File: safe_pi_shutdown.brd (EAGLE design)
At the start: 65 x 56 mm, 33 parts, among them IC1 MCP73831, IC2 LTC2952CF, IC3 MT3608, Q1 IRF7342, Q2 IRF7342, X4 MF-CON-2.54mm-01x02, X5 MF-CON-2.54mm-01x02

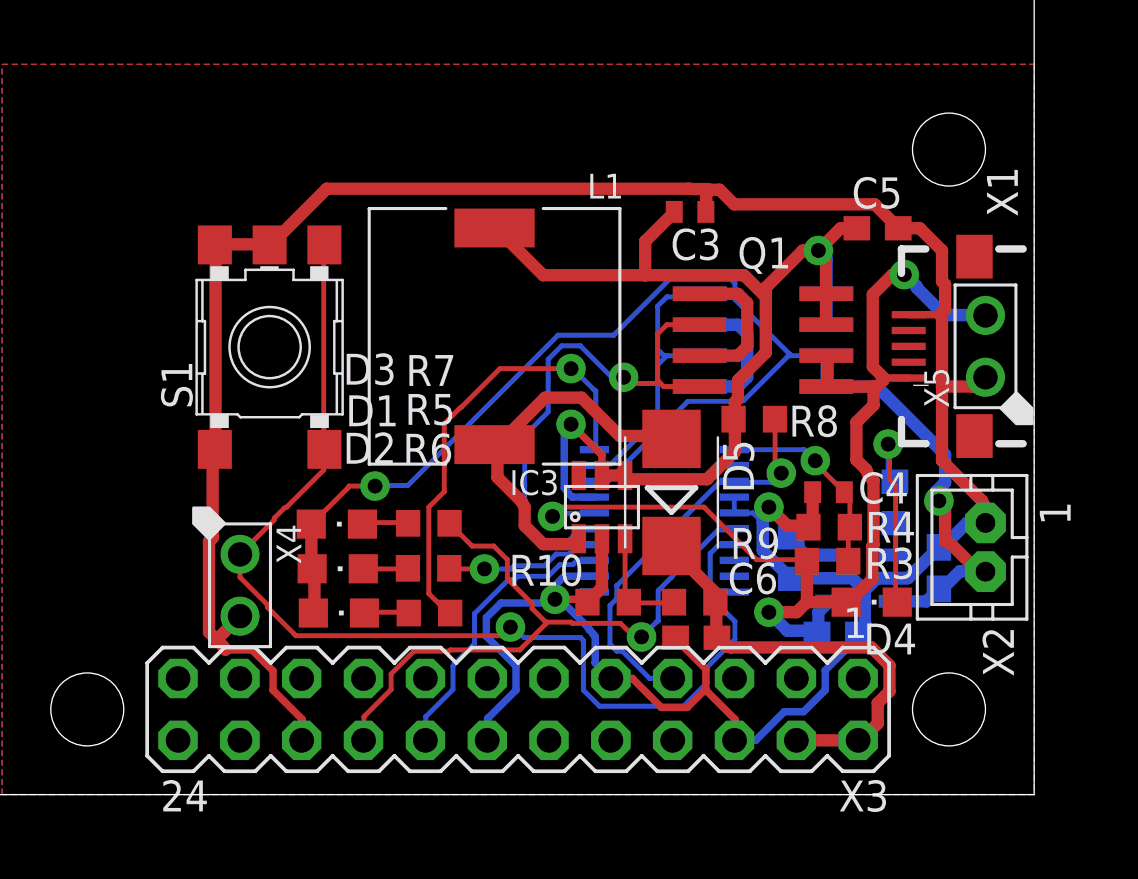
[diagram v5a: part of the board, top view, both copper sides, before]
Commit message: zmiana micro usb, poprawki z kondensatorami i inne
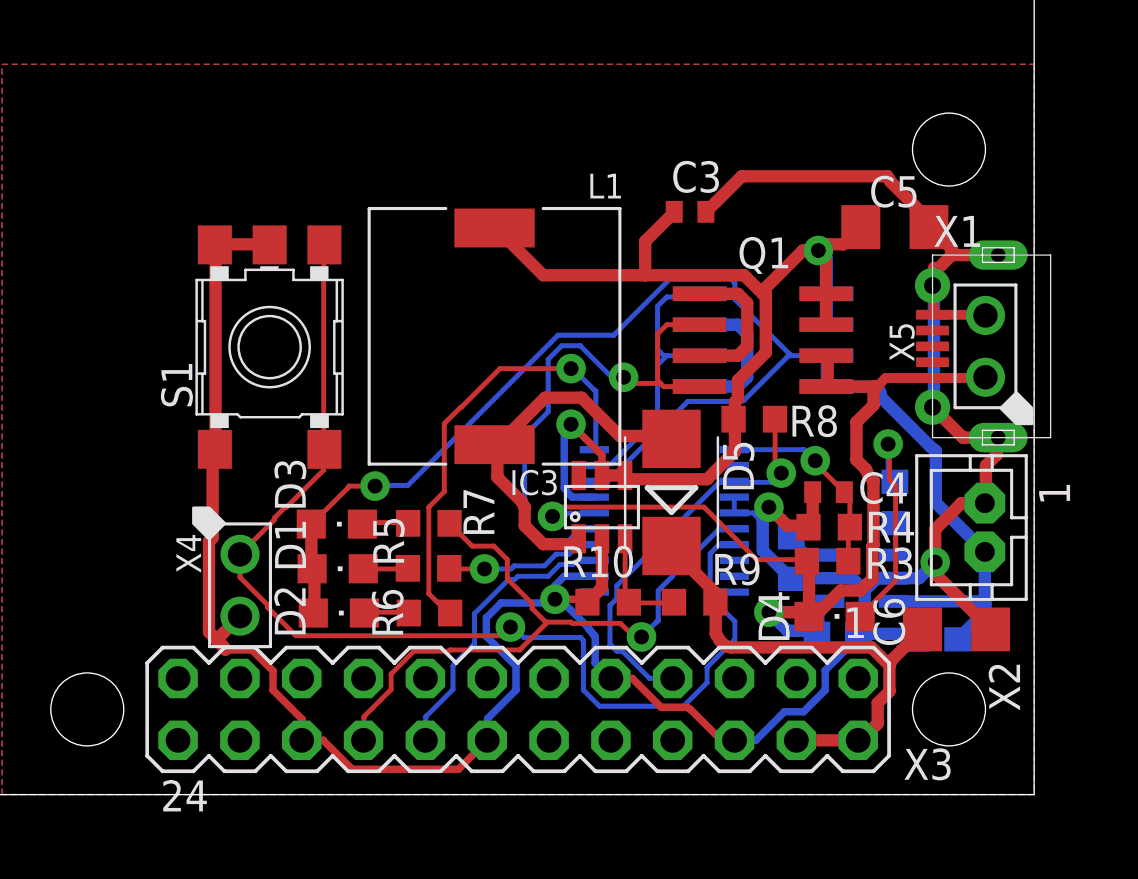
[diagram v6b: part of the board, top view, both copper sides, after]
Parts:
- C5, C6: device rcl:C0603 -> rcl:C1206
- X1: value (none) -> MICRO-USB-RECEPTACLE47589-0001; device MicroUSB:USB-MICRO-SMD -> con-molex-usb:47589-0001
- moved C6 10.7 mm to (61.8, 6.79), turned to 0 degrees
- moved C2 2.93 mm to (61.0, 6.38), turned to 0 degrees
- moved D4 1.63 mm to (56.8, 7.32)
- moved X1 0.98 mm to (63.5, 18.4)
- moved X2 0.81 mm to (63.0, 11.0)
- moved C5 0.71 mm to (59.3, 23.3)
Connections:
- net GND: now also X1.5, X1.CASING1, X1.CASING2, X1.CASING3, X1.CASING4, X5.P$2; no longer X1.GND1, X5.P$1
- net V2: now also X1.1, X5.P$1; no longer X1.VBUS1, X5.P$2
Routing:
- net V2: track 46.5 -> 41.1 mm, vias 3 -> 2
- net GND: track 131.0 -> 128.5 mm, vias 2 -> 3
- net V1: track 58.8 -> 61.0 mm, vias 2 -> 1
- net N$4: track 18.3 -> 20.3 mm
- net N$6: track 8.43 -> 9.59 mm
- net VCC: track 47.3 -> 47.9 mm

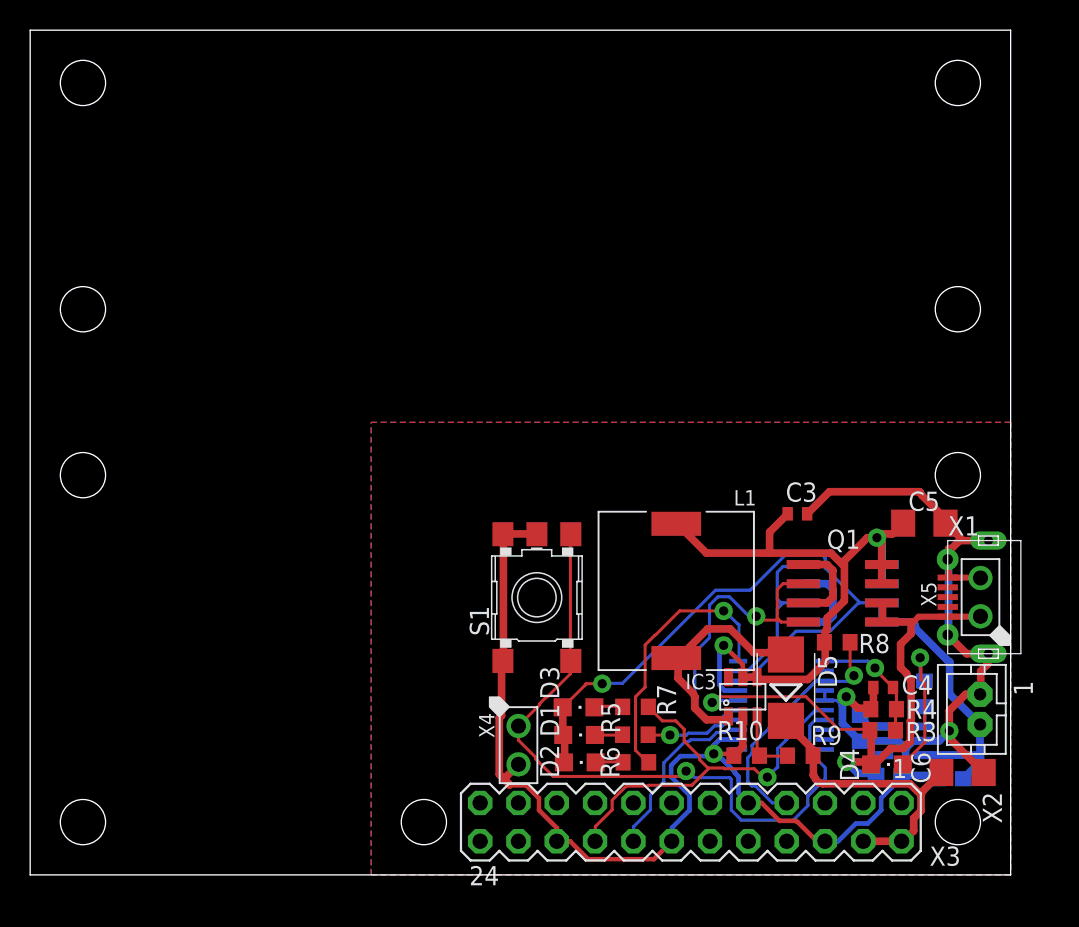
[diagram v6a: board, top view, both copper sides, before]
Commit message: przyciecie plytki do minimum
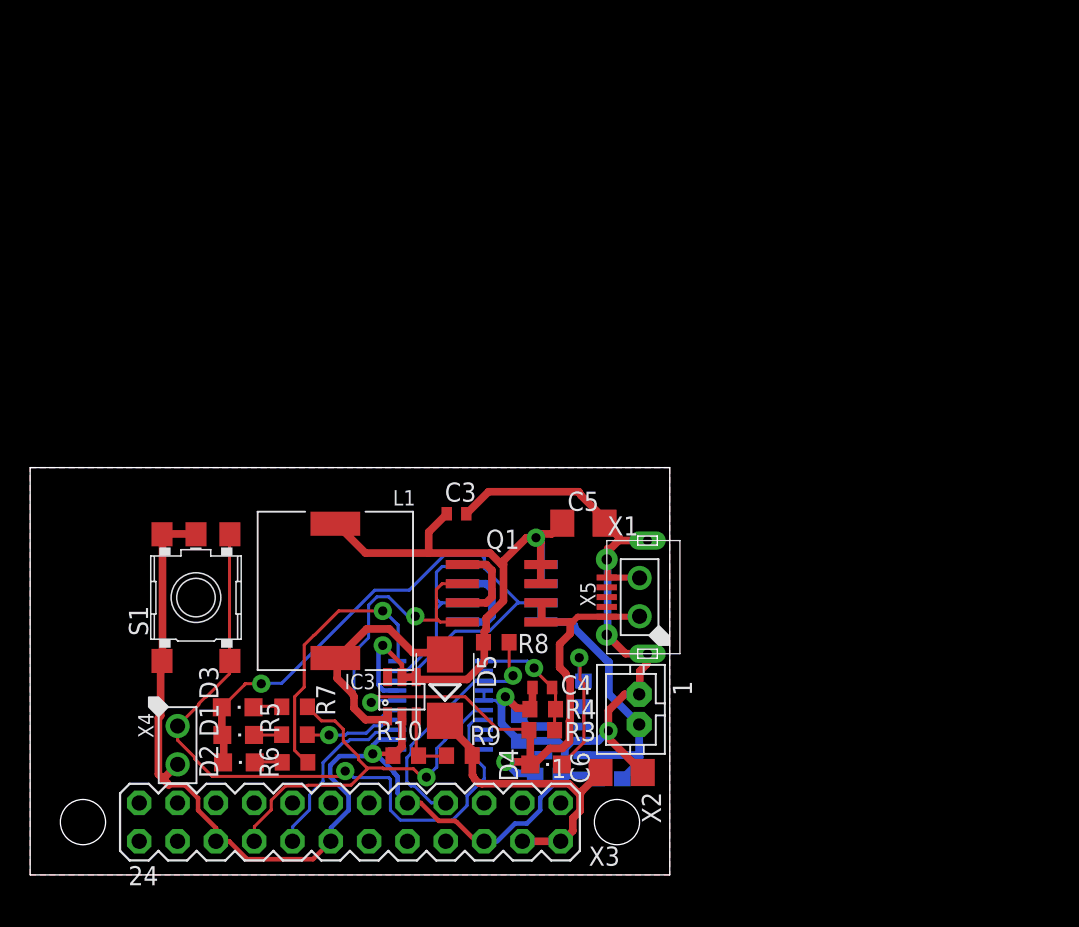
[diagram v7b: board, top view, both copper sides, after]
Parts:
- moved R5 22.6 mm to (17.5, 9.30)
- moved C1 22.6 mm to (34.3, 6.60)
- moved C2 22.6 mm to (38.4, 6.38)
- moved C3 22.6 mm to (28.3, 23.9)
- moved C5 22.6 mm to (36.7, 23.3)
- moved D1 22.6 mm to (13.8, 9.28)
- moved D2 22.6 mm to (13.8, 7.46)
- moved D4 22.6 mm to (34.2, 7.32)
- moved D5 22.6 mm to (27.5, 12.4)
- moved IC1 22.6 mm to (35.3, 8.89)
- moved IC3 22.6 mm to (24.6, 11.8)
- moved L1 22.6 mm to (20.2, 18.8)
- moved Q2 22.6 mm to (31.3, 18.7)
- moved R1 22.6 mm to (36.7, 12.0)
- moved R2 22.6 mm to (32.4, 9.72)
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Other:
- board size 65 x 56 mm -> 42.4 x 27 mm
